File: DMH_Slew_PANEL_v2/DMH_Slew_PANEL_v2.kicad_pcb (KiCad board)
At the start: 2 copper layers, 50 x 200 mm, 22 parts

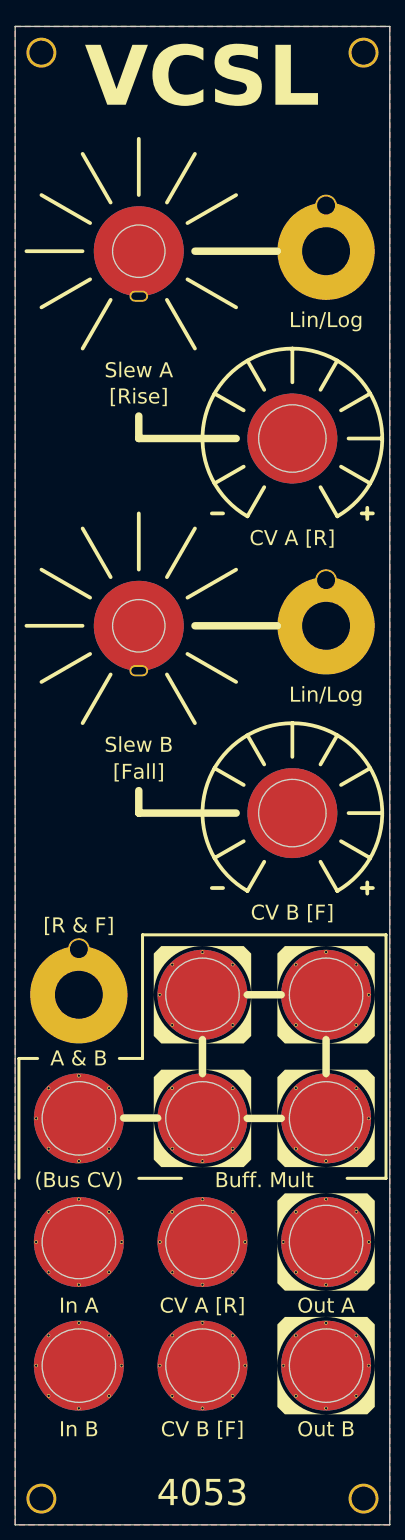
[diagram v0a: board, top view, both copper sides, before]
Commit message: Redesigned front panel in v2
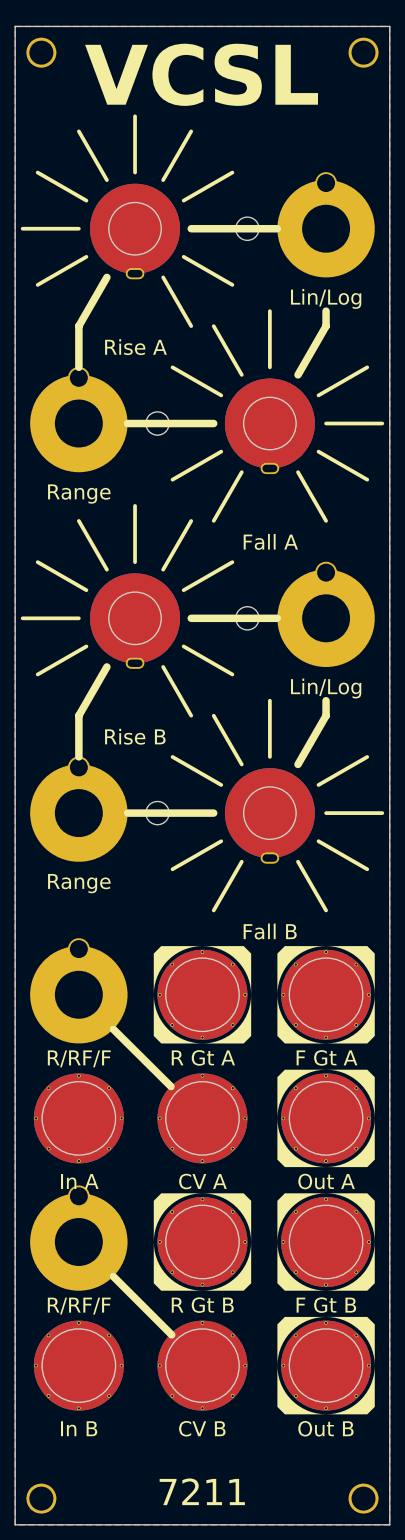
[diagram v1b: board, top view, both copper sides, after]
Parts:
- removed H12: Mult In A, SynthStuff:Jack_6.35mm_Cutout_v3
- added H24: R/RF/F, SynthStuff:Toggle_Switch_TE_Cutout, F.Cu at (58.5, 192.2)
- added H25: Range, SynthStuff:Toggle_Switch_TE_Cutout, F.Cu at (58.5, 135.0)
- added H26: Range, SynthStuff:Toggle_Switch_TE_Cutout, F.Cu at (58.5, 83.0)
- added H27: LED R A, SynthStuff:MountingHole_LED_3mm_R, F.Cu at (81.0, 57.0)
- added H28: LED R B, SynthStuff:MountingHole_LED_3mm_R, F.Cu at (81.0, 109.0)
- added H29: LED F A, SynthStuff:MountingHole_LED_3mm_Y, F.Cu at (69.0, 83.0)
- added H30: LED F B, SynthStuff:MountingHole_LED_3mm_Y, F.Cu at (69.0, 135.0)
- H13: value Mult Out A 1 -> R Gt A
- H14: value Mult Out A 2 -> F Gt A
- H15: value Mult Out B 1 -> R Gt B
- H16: value Mult Out B 2 -> F Gt B
- H17: value Slew A -> Rise A
- H18: value CV A [R] -> Fall A; footprint SynthStuff:Pot_Cutout_Tiny_attv_P110KH1 -> SynthStuff:Pot_Cutout_Small
- H19: value Slew B -> Rise B
- H20: value CV B [F] -> Fall B; footprint SynthStuff:Pot_Cutout_Tiny_attv_P110KH1 -> SynthStuff:Pot_Cutout_Small
- H23: value A & B -> R/RF/F
- H6: value CV A [R] -> CV A
- H9: value CV B [F] -> CV B
- moved H15 16.5 mm to (75.0, 192.2)
- moved H16 16.5 mm to (91.5, 192.2)
- moved H5 16.5 mm to (58.5, 175.8)
- moved H6 16.5 mm to (75.0, 175.8)
- moved H7 16.5 mm to (91.5, 175.8)
- moved H18 3.61 mm to (84.0, 83.0)
- moved H17 3.04 mm to (66.0, 57.0)
- moved H20 3.00 mm to (84.0, 135.0)
- moved H21 3.00 mm to (91.5, 57.0)
- moved H19 1.12 mm to (66.0, 109.0)
- moved H22 1.00 mm to (91.5, 109.0)
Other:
- board text added: "7211"
- board text removed: "(Bus CV)"
- board text removed: "4053"
- board text removed: "Buff. Mult"
- board text removed: "[Fall]"
- board text removed: "[R & F]"
- board text removed: "[Rise]"

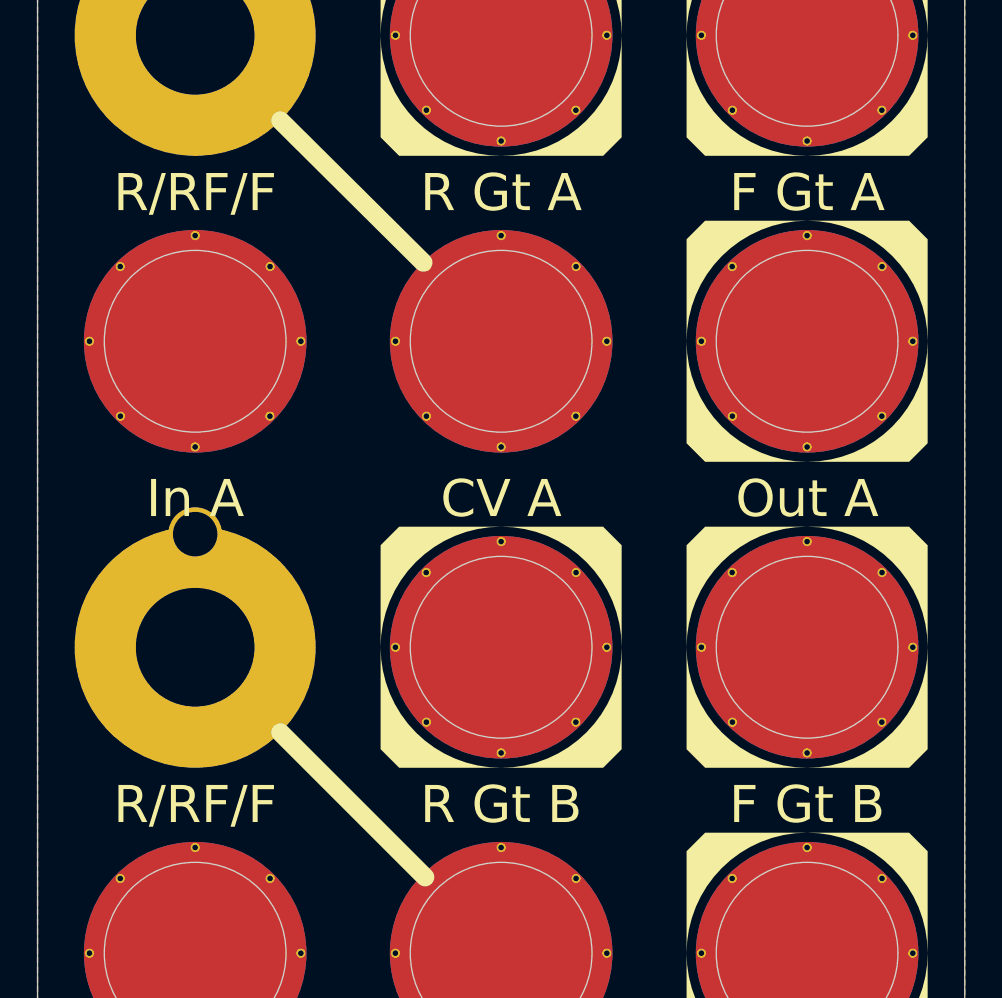
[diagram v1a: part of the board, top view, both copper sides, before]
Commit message: Separating PCB 1 and 2 in schematic
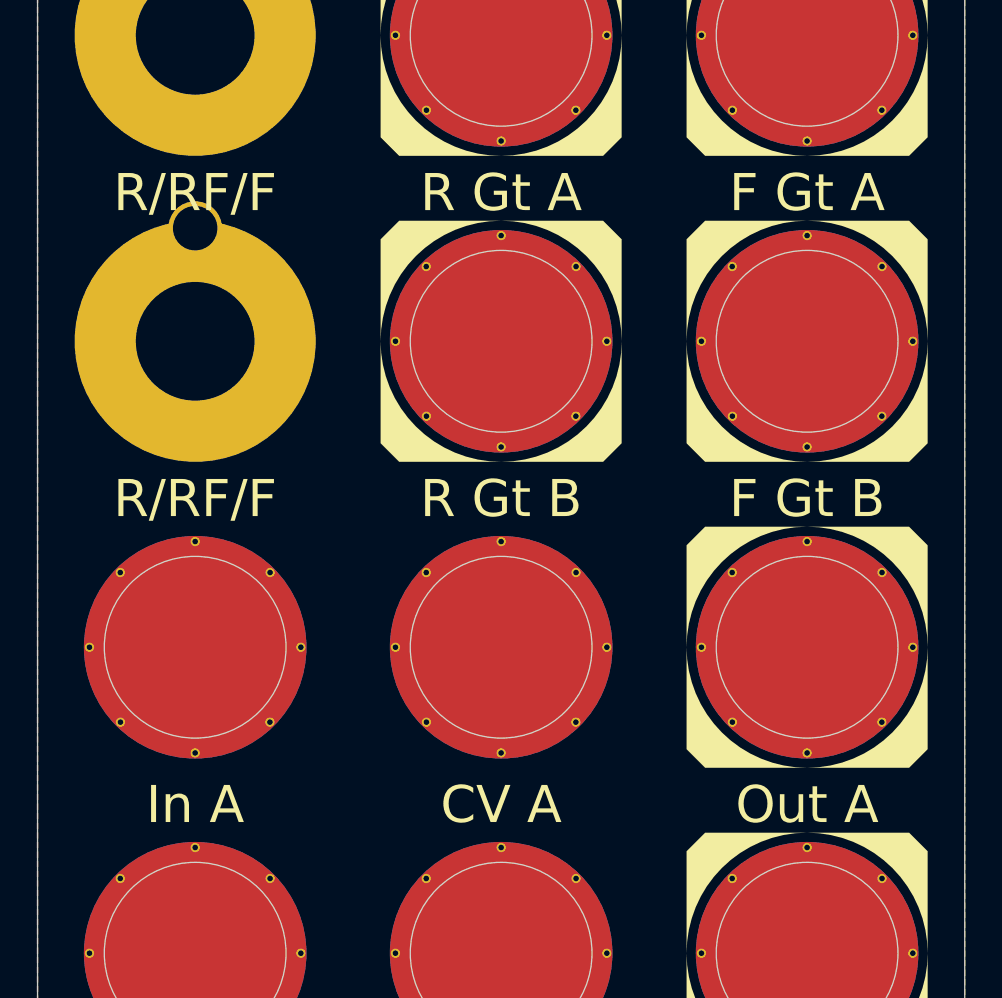
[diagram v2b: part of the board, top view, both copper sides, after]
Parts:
- moved H15 16.5 mm to (75.0, 175.8)
- moved H16 16.5 mm to (91.5, 175.8)
- moved H24 16.5 mm to (58.5, 175.8)
- moved H5 16.5 mm to (58.5, 192.2)
- moved H6 16.5 mm to (75.0, 192.2)
- moved H7 16.5 mm to (91.5, 192.2)

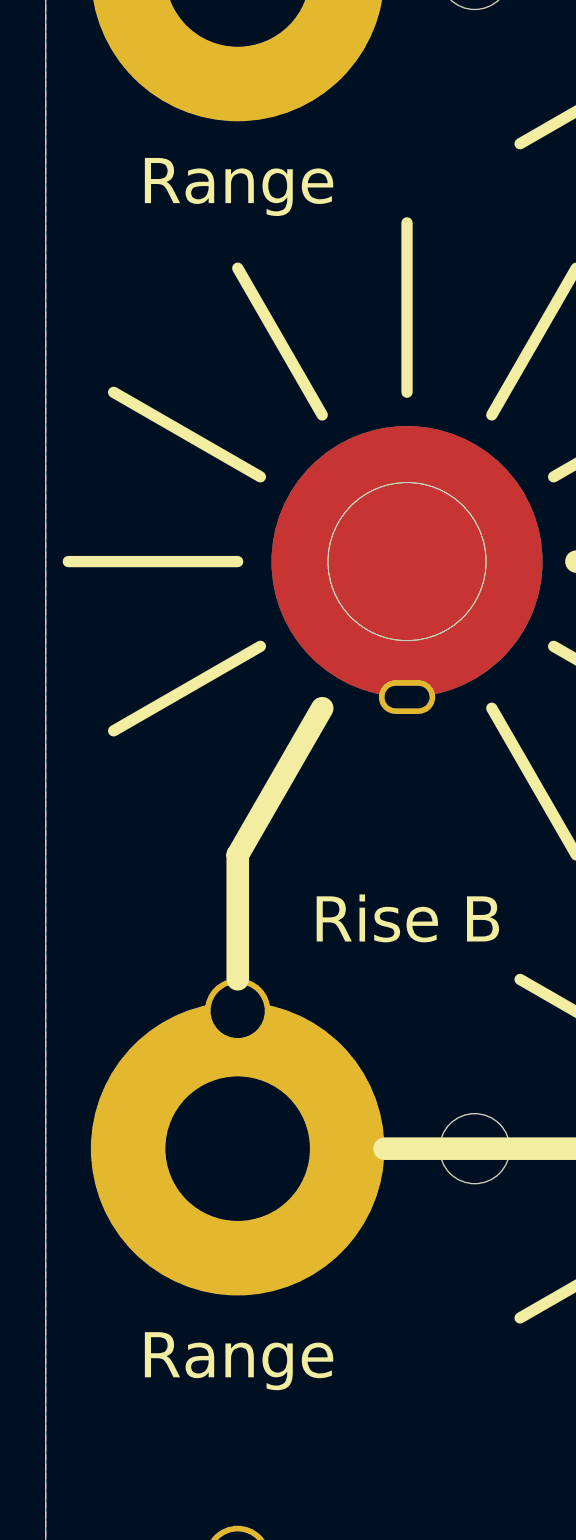
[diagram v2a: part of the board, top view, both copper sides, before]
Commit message: PCB 2 component placement done
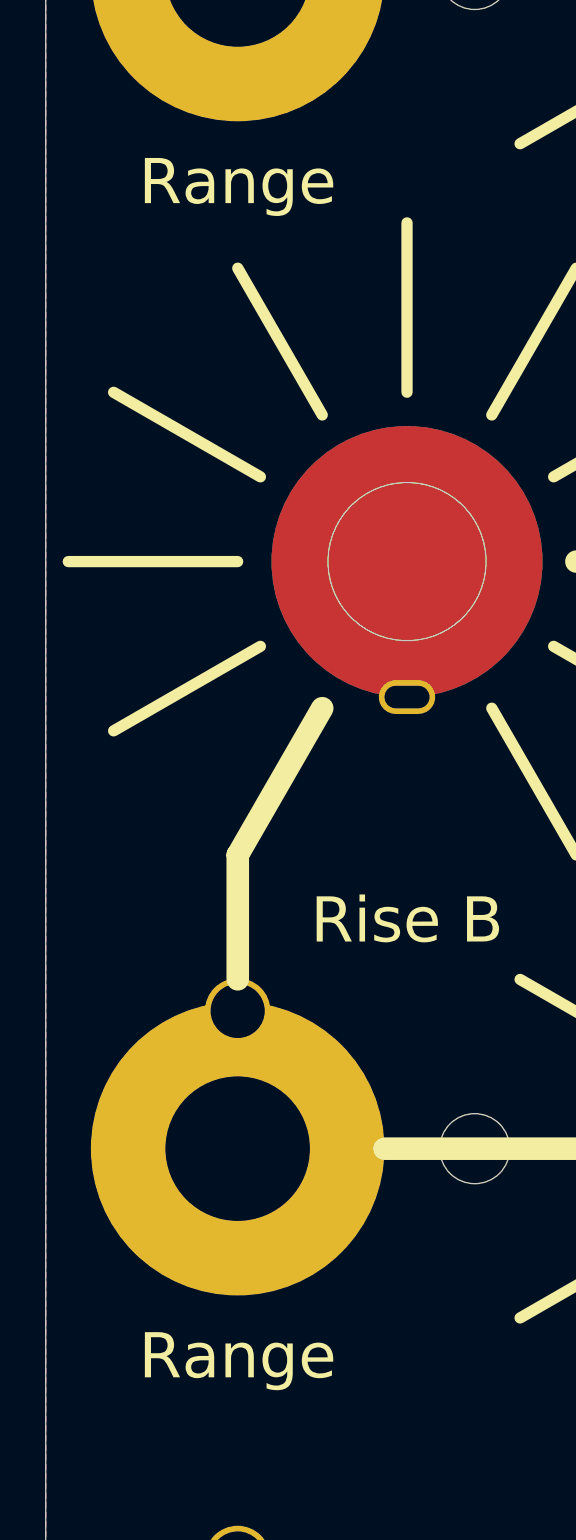
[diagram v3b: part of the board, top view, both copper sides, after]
